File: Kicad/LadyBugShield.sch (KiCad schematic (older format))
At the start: 4 parts, among them P1 CONN_6, P2 CONN_2, P3 BNC, P4 BNC

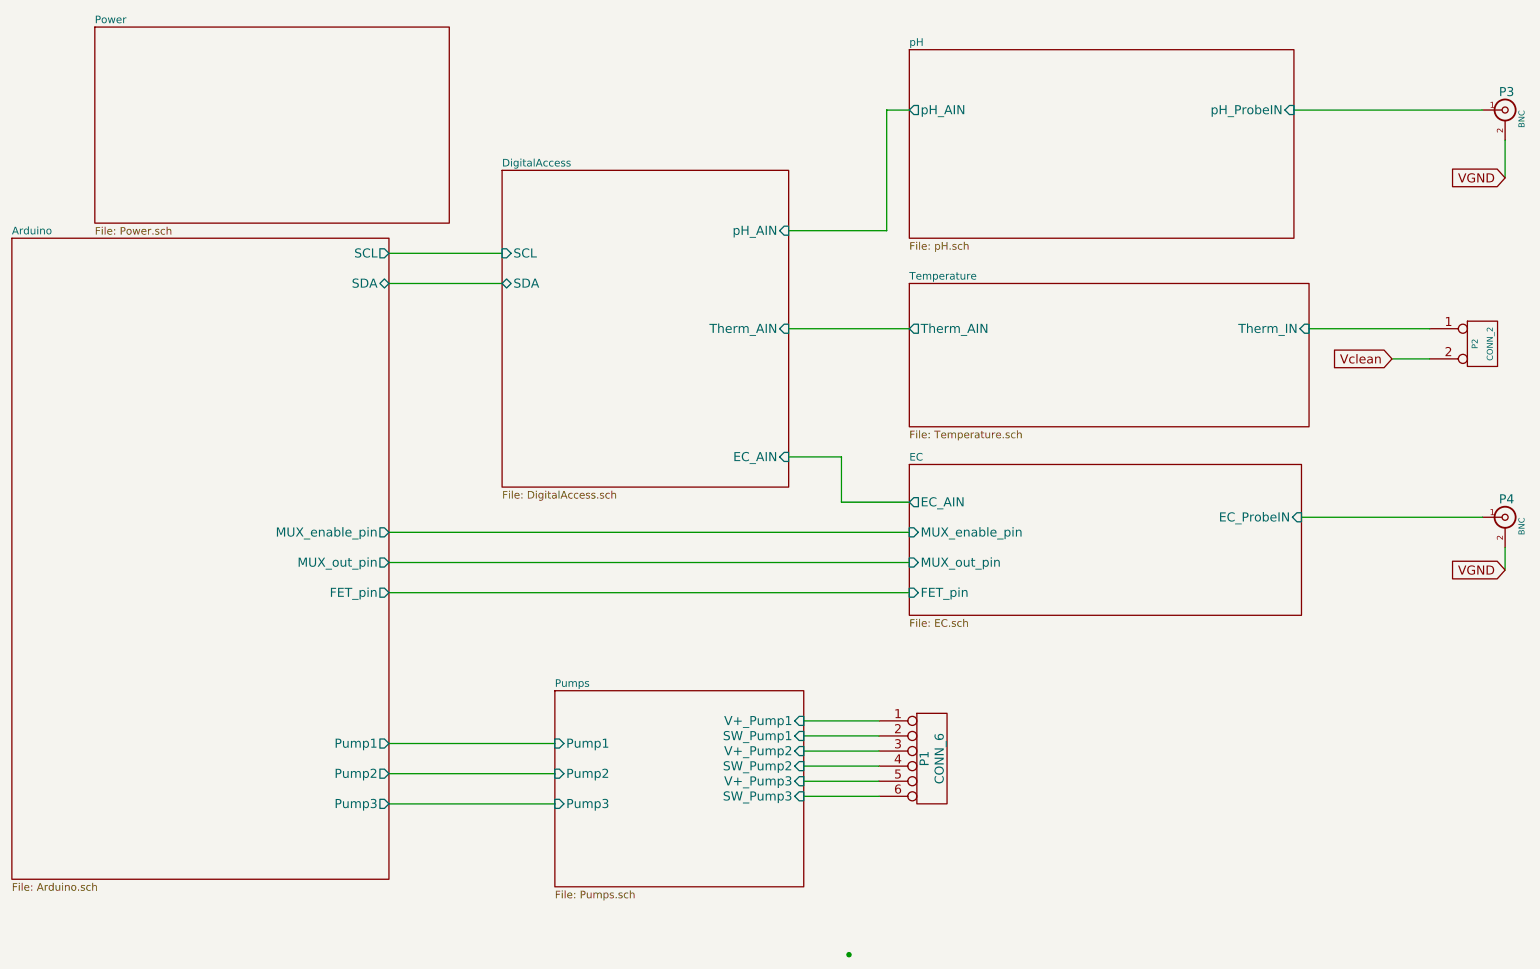
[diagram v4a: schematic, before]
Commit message: iPhone app and changes to hw design (not sure I like)
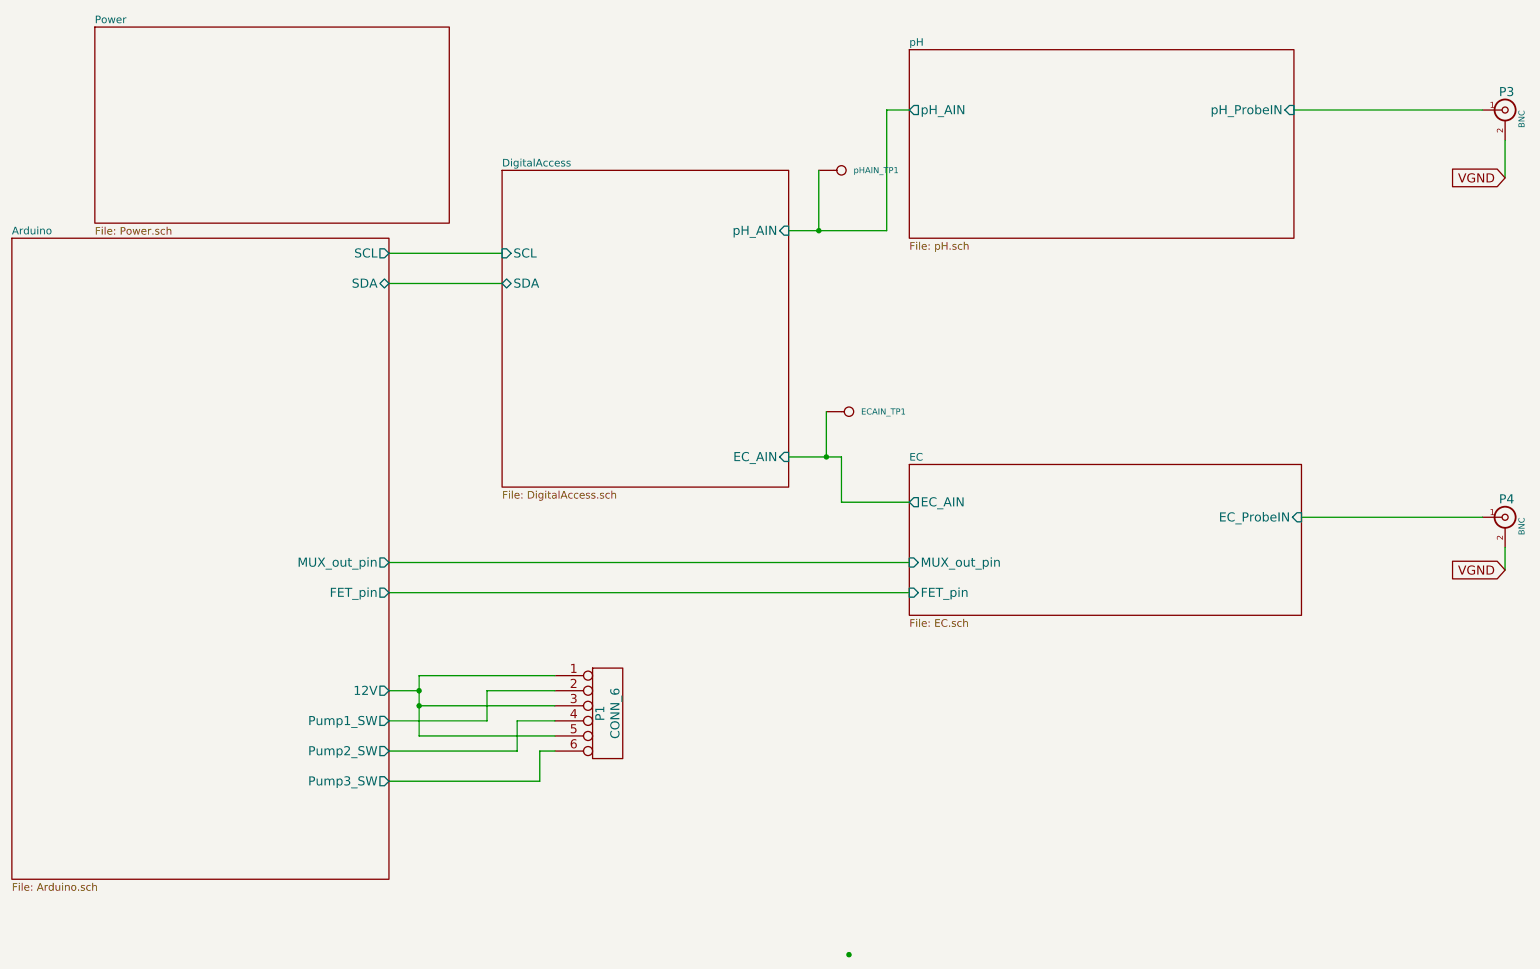
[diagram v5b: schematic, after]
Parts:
- removed P2: CONN_2, symbol CONN_2
- added ECAIN_TP1, pHAIN_TP1: CONN_1, symbol CONN_1
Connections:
- net Pumps/V+_Pump2 is gone; now on net Arduino/12V: P1.3
- net Pumps/V+_Pump3 is gone; now on net Arduino/12V: P1.5
- net DigitalAccess/EC_AIN: now also ECAIN_TP1.1
- net DigitalAccess/pH_AIN: now also pHAIN_TP1.1
- net Pumps/SW_Pump1 renamed Arduino/Pump1_SW
- net Pumps/SW_Pump2 renamed Arduino/Pump2_SW
- net Pumps/SW_Pump3 renamed Arduino/Pump3_SW
- net Pumps/V+_Pump1 renamed Arduino/12V
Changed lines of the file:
@@
 $Descr A4 11693 8268
 encoding utf-8
-Sheet 1 11
+Sheet 1 9
 Title ""
-Date "9 feb 2015"
+Date "17 mar 2015"
 Rev ""
 Comp ""
@@
 F2 "SDA" B R 3300 2400 60
 F3 "SCL" O R 3300 2200 60
-F4 "Pump2" O R 3300 5650 60
-F5 "Pump1" O R 3300 5450 60
-F6 "Pump3" O R 3300 5850 60
-F7 "MUX_out_pin" O R 3300 4250 60
-F8 "FET_pin" O R 3300 4450 60
-F9 "MUX_enable_pin" O R 3300 4050 60
+F4 "MUX_out_pin" O R 3300 4250 60
+F5 "FET_pin" O R 3300 4450 60
+F6 "12V" O R 3300 5100 60
+F7 "Pump1_SW" O R 3300 5300 60
+F8 "Pump2_SW" O R 3300 5500 60
+F9 "Pump3_SW" O R 3300 5700 60
 $EndSheet
 $Sheet
@@
 F4 "pH_AIN" I R 5950 2050 60
 F5 "EC_AIN" I R 5950 3550 60
-F6 "Therm_AIN" I R 5950 2700 60
 $EndSheet
 $Sheet
@@
 F4 "MUX_out_pin" I L 6750 4250 60
 F5 "FET_pin" I L 6750 4450 60
-F6 "MUX_enable_pin" I L 6750 4050 60
 $EndSheet
 $Sheet
@@
 Wire Wire Line
 	9300 1250 10550 1250
-Wire Wire Line
-	9400 2700 10200 2700
 Wire Wire Line
 	6750 1250 6600 1250
@@
 	3300 2400 4050 2400
 Connection ~ 6350 6850
-$Sheet
-S 6750 2400 2650 950
-U 547DE6A0
-F0 "Temperature" 50
-F1 "Temperature.sch" 50
-F2 "Therm_IN" I R 9400 2700 60
-F3 "Therm_AIN" O L 6750 2700 60
-$EndSheet
 Text GLabel 10700 1700 0    60   Input ~ 0
 VGND
 Text GLabel 10700 4300 0    60   Input ~ 0
 VGND
-Text GLabel 9950 2900 0    60   Input ~ 0
-Vclean
 $Comp
 L BNC P3
@@
 	1    0    0    -1
 $EndComp
-$Comp
-L CONN_2 P2
-U 1 1 54903E39
-P 10550 2800
-F 0 "P2" V 10500 2800 40  0000 C CNN
-F 1 "CONN_2" V 10600 2800 40  0000 C CNN
-F 2 "" H 10550 2800 60  0000 C CNN
-F 3 "" H 10550 2800 60  0000 C CNN
-	1    10550 2800
-	1    0    0    -1
-$EndComp
-$Comp
-L CONN_6 P1
-U 1 1 54903E48
-P 6900 5550
-F 0 "P1" V 6850 5550 60  0000 C CNN
-F 1 "CONN_6" V 6950 5550 60  0000 C CNN
-F 2 "" H 6900 5550 60  0000 C CNN
-F 3 "" H 6900 5550 60  0000 C CNN
-	1    6900 5550
-	1    0    0    -1
-$EndComp
 Wire Wire Line
 	10700 1450 10700 1700
@@
 	10700 4150 10700 4300
 Wire Wire Line
-	3300 5450 4400 5450
-Wire Wire Line
-	3300 5650 4400 5650
-Wire Wire Line
-	3300 5850 4400 5850
-$Sheet
-S 4400 5100 1650 1300
-U 547DE6BF
-F0 "Pumps" 50
-F1 "Pumps.sch" 50
-F2 "Pump1" I L 4400 5450 60
-F3 "V+_Pump1" I R 6050 5300 60
-F4 "SW_Pump1" I R 6050 5400 60
-F5 "Pump2" I L 4400 5650 60
-F6 "SW_Pump2" I R 6050 5600 60
-F7 "V+_Pump2" I R 6050 5500 60
-F8 "Pump3" I L 4400 5850 60
-F9 "SW_Pump3" I R 6050 5800 60
-F10 "V+_Pump3" I R 6050 5700 60
-$EndSheet
-Wire Wire Line
-	9950 2900 10200 2900
-Wire Wire Line
-	6550 5300 6050 5300
-Wire Wire Line
-	6050 5400 6550 5400
-Wire Wire Line
-	6050 5500 6550 5500
-Wire Wire Line
-	6050 5600 6550 5600
-Wire Wire Line
-	6050 5700 6550 5700
-Wire Wire Line
-	6050 5800 6550 5800
-Wire Wire Line
-	5950 2700 6750 2700
-Wire Wire Line
 	6750 3850 6300 3850
 Wire Wire Line
@@
 	6300 3550 5950 3550
 Wire Wire Line
-	3300 4050 6750 4050
-Wire Wire Line
 	3300 4250 6750 4250
 Wire Wire Line
 	3300 4450 6750 4450
+$Comp
+L CONN_6 P1
+U 1 1 550579A6
+P 4750 5250
+F 0 "P1" V 4700 5250 60  0000 C CNN
+F 1 "CONN_6" V 4800 5250 60  0000 C CNN
+F 2 "" H 4750 5250 60  0000 C CNN
+F 3 "" H 4750 5250 60  0000 C CNN
+	1    4750 5250
+	1    0    0    -1
+$EndComp
+$Comp
+L CONN_1 pHAIN_TP1
+U 1 1 5506C613
+P 6300 1650
+F 0 "pHAIN_TP1" H 6380 1650 40  0000 L CNN
+F 1 "CONN_1" H 6300 1705 30  0001 C CNN
+F 2 "" H 6300 1650 60  0000 C CNN
+F 3 "" H 6300 1650 60  0000 C CNN
+	1    6300 1650
+	1    0    0    -1
+$EndComp
+Wire Wire Line
+	6150 1650 6150 2050
+Connection ~ 6150 2050
+$Comp
+L CONN_1 ECAIN_TP1
+U 1 1 5506C6CE
+P 6350 3250
+F 0 "ECAIN_TP1" H 6430 3250 40  0000 L CNN
+F 1 "CONN_1" H 6350 3305 30  0001 C CNN
+F 2 "" H 6350 3250 60  0000 C CNN
+F 3 "" H 6350 3250 60  0000 C CNN
+	1    6350 3250
+	1    0    0    -1
+$EndComp
+Wire Wire Line
+	6200 3250 6200 3550
+Connection ~ 6200 3550
+Wire Wire Line
+	4400 5000 3500 5000
+Wire Wire Line
+	3500 5000 3500 5400
+Wire Wire Line
+	3500 5100 3300 5100
+Wire Wire Line
+	3500 5200 4400 5200
+Connection ~ 3500 5100
+Wire Wire Line
+	3500 5400 4400 5400
+Connection ~ 3500 5200
+Wire Wire Line
+	3300 5300 3950 5300
+Wire Wire Line
+	3950 5300 3950 5100
+Wire Wire Line
+	3950 5100 4400 5100
+Wire Wire Line
+	3300 5500 4150 5500
+Wire Wire Line
+	4150 5500 4150 5300
+Wire Wire Line
+	4150 5300 4400 5300
+Wire Wire Line
+	3300 5700 4300 5700
+Wire Wire Line
+	4300 5700 4300 5500
+Wire Wire Line
+	4300 5500 4400 5500
 $EndSCHEMATC
